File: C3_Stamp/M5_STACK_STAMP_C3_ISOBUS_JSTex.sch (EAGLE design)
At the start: 13 parts, among them IC1 MCP2562-E_P, J2 61300611121, J3 61301621821, X1 S4P-VH

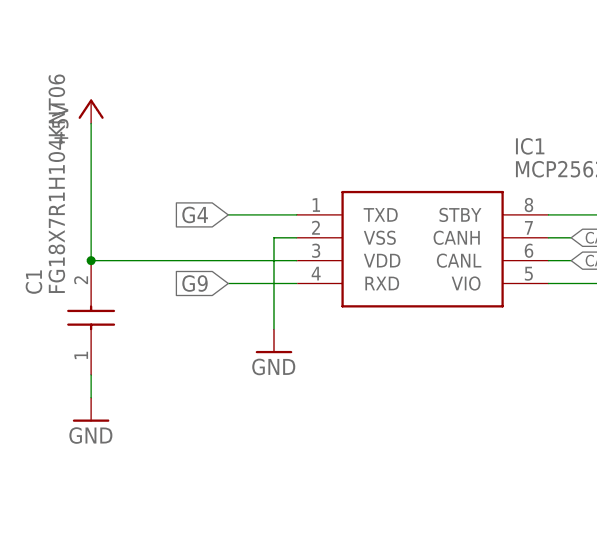
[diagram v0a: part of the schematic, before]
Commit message: G7 for CAN RX, as G9 is a Strapping Pin.
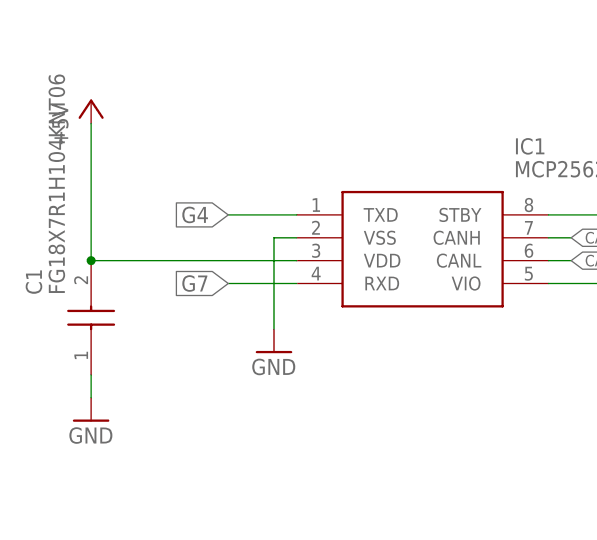
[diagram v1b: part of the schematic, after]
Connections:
- net G7: now also IC1.RXD
- net G9: no longer IC1.RXD
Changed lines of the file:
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@@
 <label x="40.64" y="88.9" size="1.27" layer="95" xref="yes"/>
-</segment>
-<segment>
-<pinref part="IC1" gate="G$1" pin="RXD"/>
-<wire x1="2.54" y1="25.4" x2="-5.08" y2="25.4" width="0.1524" layer="91"/>
-<label x="-5.08" y="25.4" size="1.778" layer="95" rot="R180" xref="yes"/>
 </segment>
 </net>
@@
 <junction x="2.54" y="91.44"/>
 </segment>
+<segment>
+<pinref part="IC1" gate="G$1" pin="RXD"/>
+<wire x1="2.54" y1="25.4" x2="-5.08" y2="25.4" width="0.1524" layer="91"/>
+<label x="-5.08" y="25.4" size="1.778" layer="95" rot="R180" xref="yes"/>
+</segment>
 </net>
